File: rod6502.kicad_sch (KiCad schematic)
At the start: 5 parts, among them J1 Conn_01x08_Socket, J2 Conn_01x08_Socket, U1 W65C02SxP, X1 1MHz

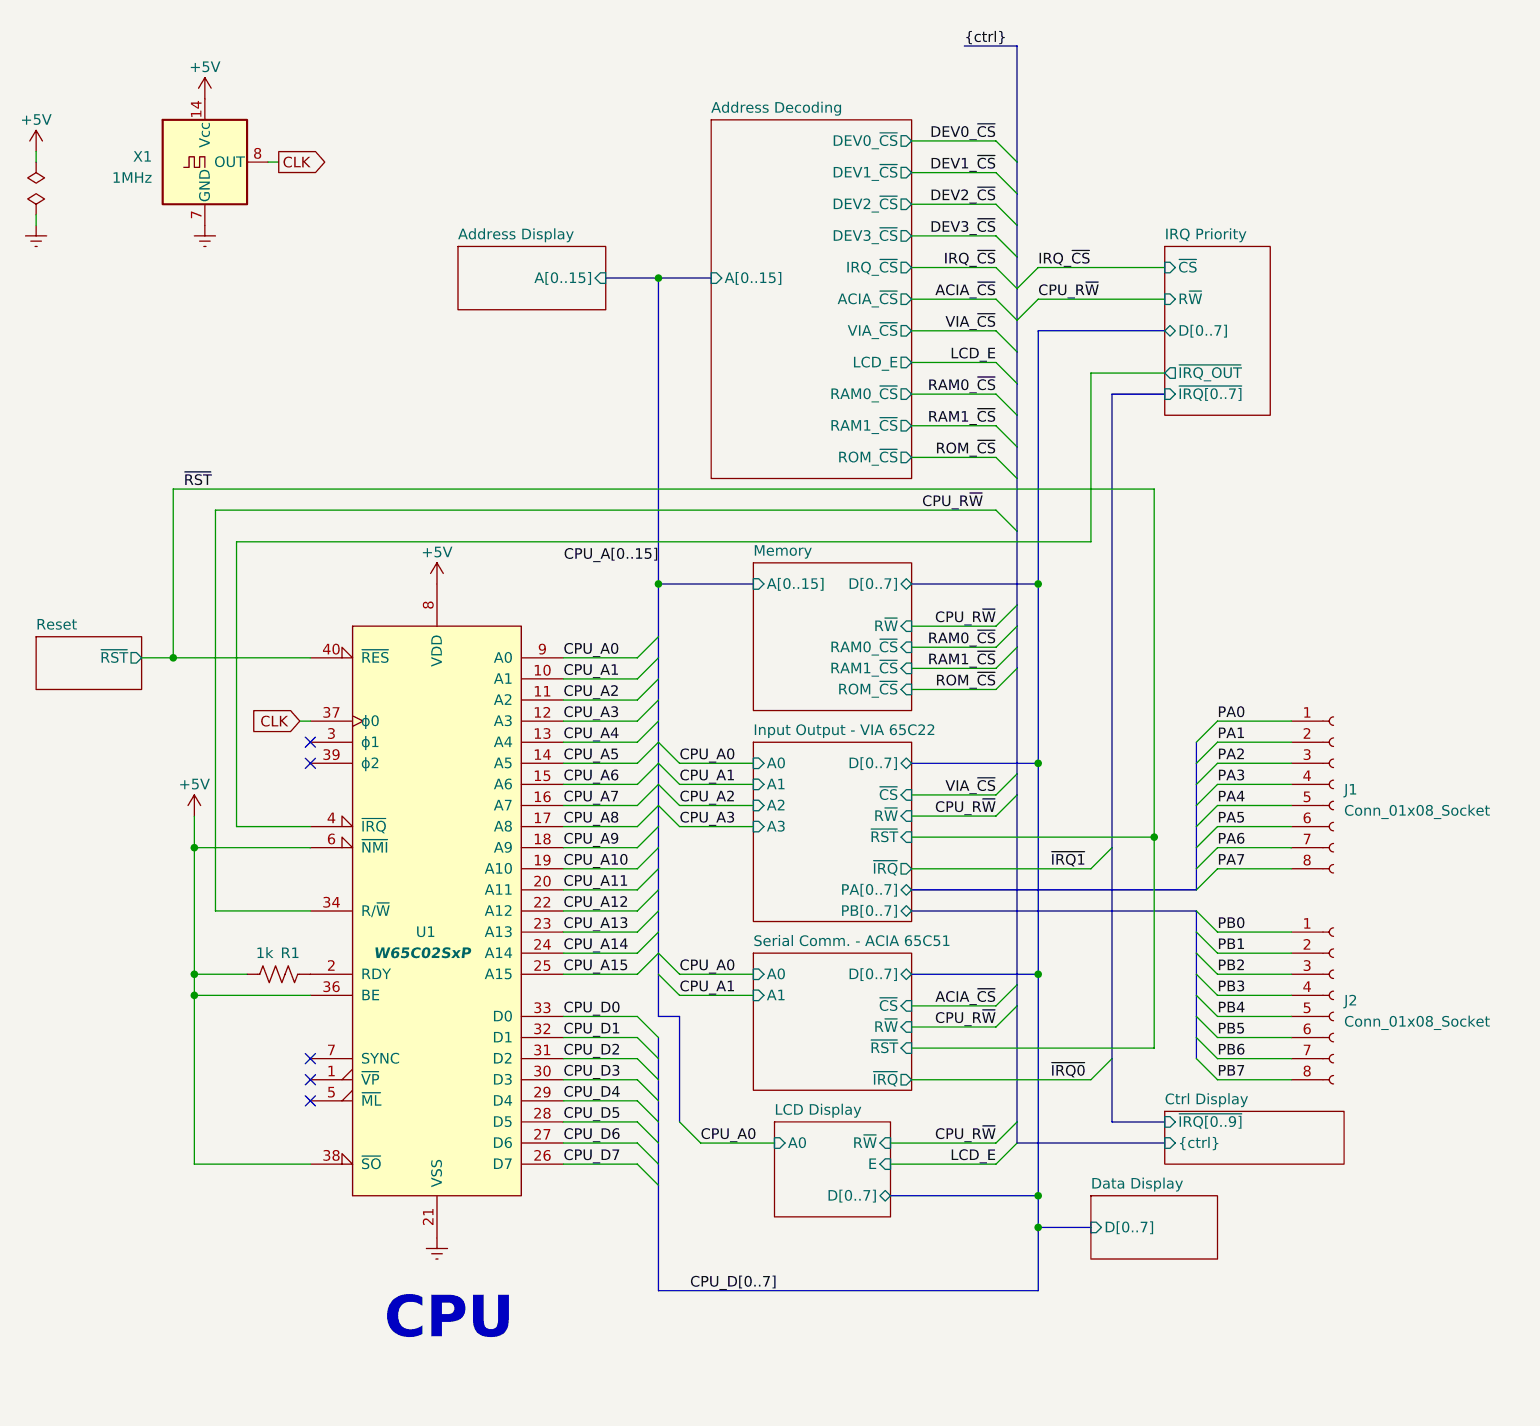
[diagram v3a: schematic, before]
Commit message: RS-232/ACIA works!
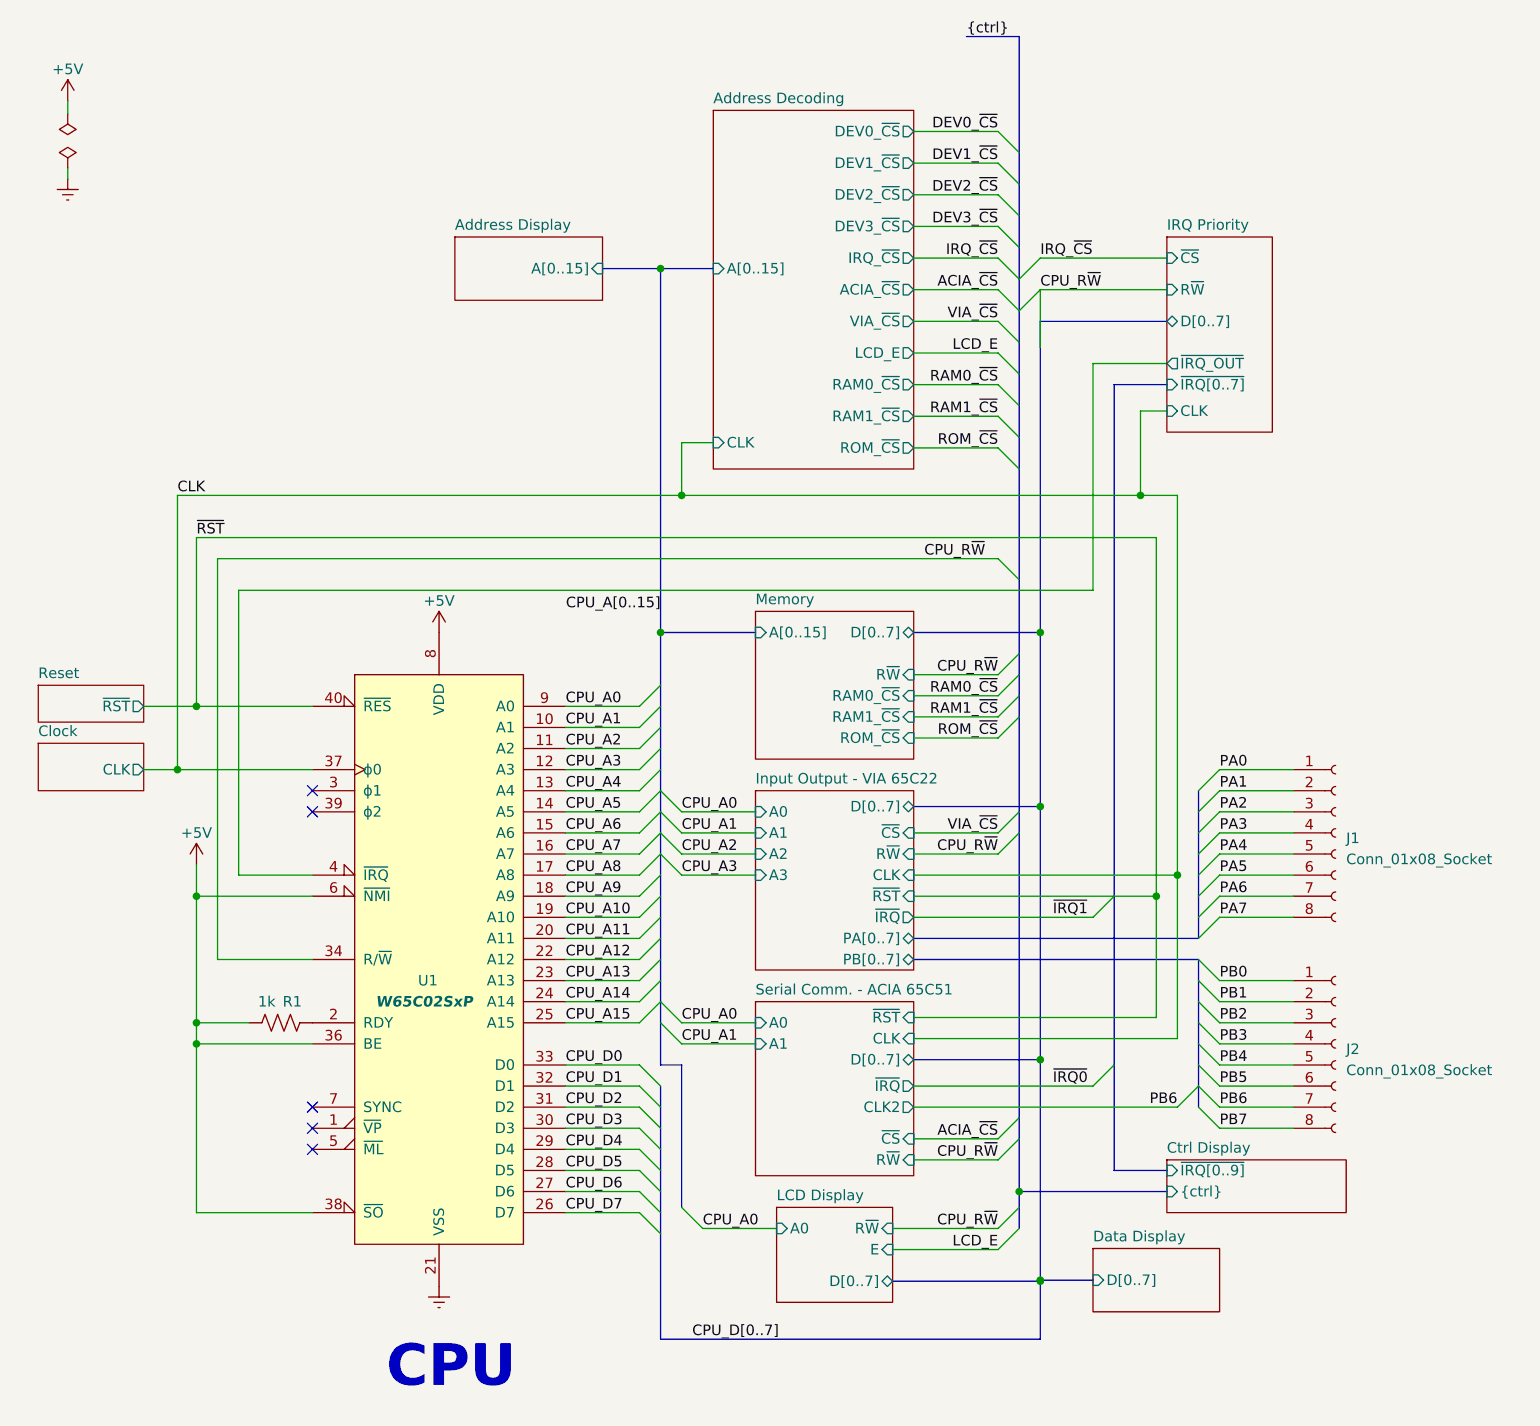
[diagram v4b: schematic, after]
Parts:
- removed X1: 1MHz, Oscillator:Oscillator_DIP-14, symbol Oscillator:ACO-xxxMHz
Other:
- added sheet Clock (clock.kicad_sch)
- sheet Address Decoding ports: added CLK; removed none
- sheet IRQ Priority ports: added CLK; removed none
- sheet Input Output - VIA 65C22 ports: added CLK; removed none
- sheet Serial Comm. - ACIA 65C51 ports: added CLK, CLK2; removed none
- moved on the sheet: J1, J2, R1, U1

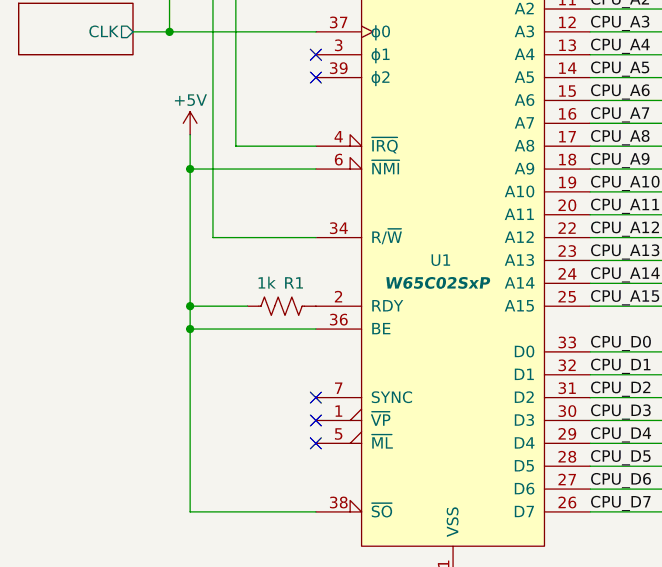
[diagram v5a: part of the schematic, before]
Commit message: acia putchar and getchar works
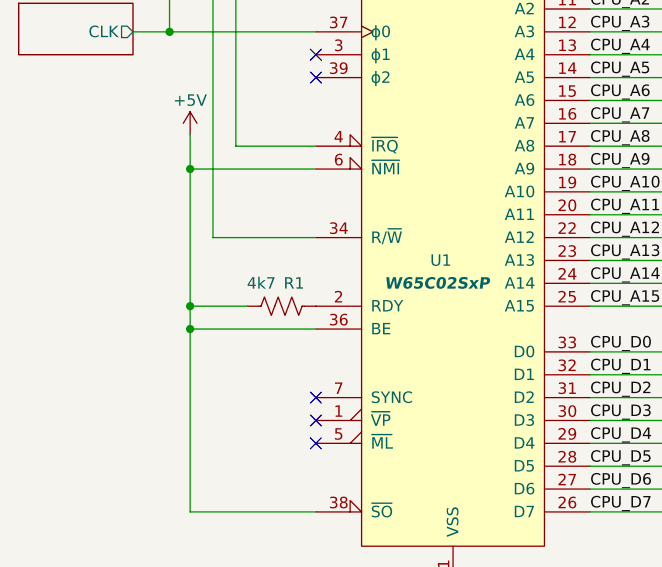
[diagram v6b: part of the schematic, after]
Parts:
- R1: value 1k -> 4k7
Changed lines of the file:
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@@
 (kicad_sch (version 20230121) (generator eeschema)
   (paper "A4")
+  (bus_alias "ctrl" (members "RAM0_~{CS}" "ROM_~{CS}" "VIA_~{CS}" "CPU_R~{W}" "ACIA_~{CS}" "IRQ_~{CS}" "LCD_E" "RAM1_~{CS}" "DEV0_~{CS}" "DEV1_~{CS}" "DEV2_~{CS}" "DEV3_~{CS}"))
   (bus_alias "cpu" (members "CPU_~{VP}" "CPU_~{ML}" "CPU_SYNC" "CPU_~{NMI}"))
-  (bus_alias "ctrl" (members "RAM0_~{CS}" "ROM_~{CS}" "VIA_~{CS}" "CPU_R~{W}" "ACIA_~{CS}" "IRQ_~{CS}" "LCD_E" "RAM1_~{CS}" "DEV0_~{CS}" "DEV1_~{CS}" "DEV2_~{CS}" "DEV3_~{CS}"))
   (bus_alias "irq" (members "~{IRQ[0..7]}" "CPU_~{IRQ}"))
   (junction (at 149.479 71.882) (diameter 0) (color 0 0 0 0)
@@
       (effects (font (size 1.27 1.27)) (justify left))
     )
-    (property "Value" "1k" (at 45.339 132.842 90)
+    (property "Value" "4k7" (at 45.339 132.842 90)
       (effects (font (size 1.27 1.27)) (justify left))
     )
